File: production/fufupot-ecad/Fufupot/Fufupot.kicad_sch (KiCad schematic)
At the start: 56 parts, among them IC1 FOD3150, J1 Conn_01x04_Pin, J1 USB_B, J10 Conn_01x03, J3 Conn_01x03, J4 Conn_01x02_Pin, J5 Conn_01x02_Pin, J6 Conn_01x03_Pin, J7 Conn_01x02_Pin, J9 Conn_01x04_Pin, SW1 SW_Push, U1 STGP8NC60KD, U2 FT232RL, U2 LM5165DRC, U3 USBLC6-2SC6, U4 ATMEGA328P-PN

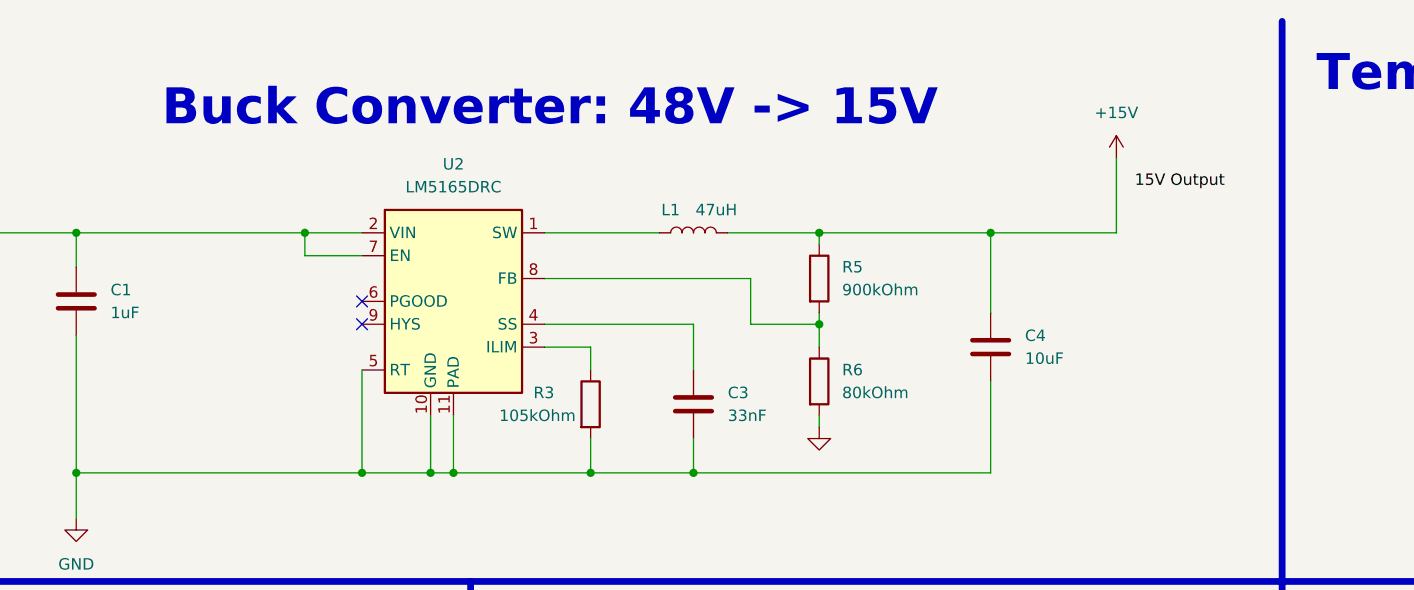
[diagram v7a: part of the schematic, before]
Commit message: Power Symbol and footprints
Made +16V power symbol and added footprints.
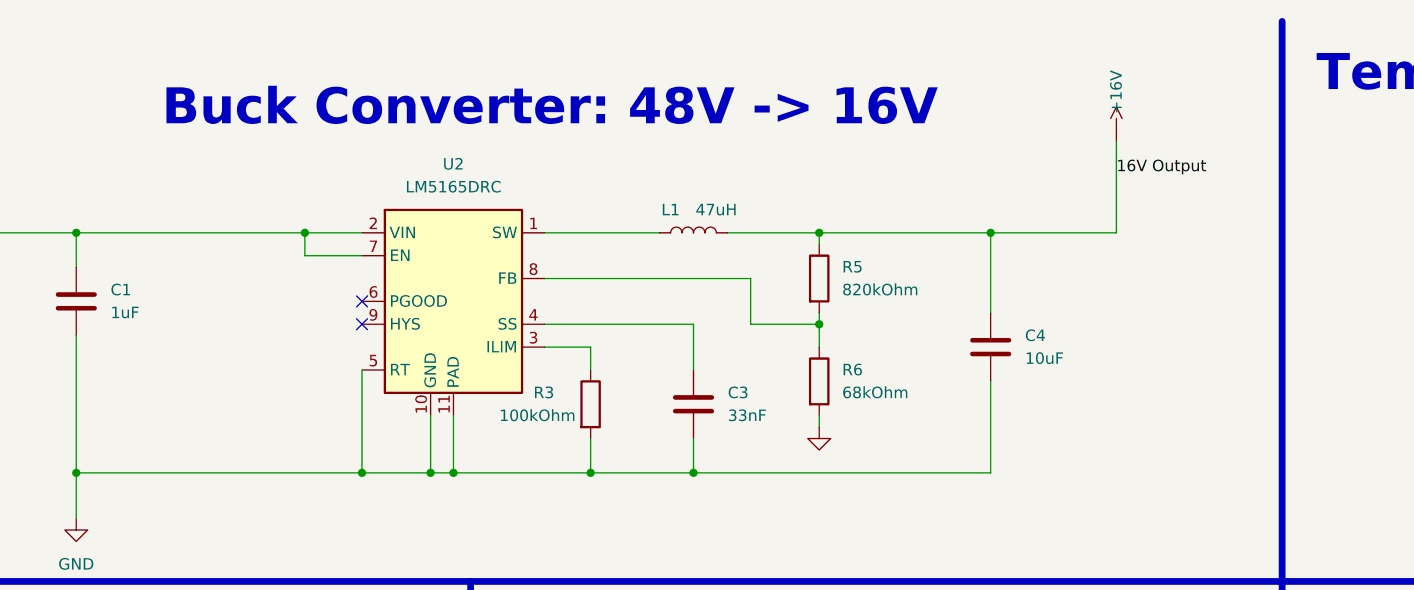
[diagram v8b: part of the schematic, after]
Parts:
- C1, C3, C4: footprint (none) -> Capacitor_SMD:C_0805_2012Metric
- L1: footprint (none) -> Inductor_SMD:L_0805_2012Metric
- R3: value 105kOhm -> 100kOhm; footprint (none) -> Resistor_SMD:R_0805_2012Metric
- R5: value 900kOhm -> 820kOhm; footprint (none) -> Resistor_SMD:R_0805_2012Metric
- R6: value 80kOhm -> 68kOhm; footprint (none) -> Resistor_SMD:R_0805_2012Metric
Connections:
- net +15V: no longer C4.1, L1.2, R5.1
- new net +16V: C4.1, L1.2, R5.1
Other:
- note added: "Buck Converter: 48V -> 16V"
- note removed: "Buck Converter: 48V -> 15V"
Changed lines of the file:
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@@
     (stroke (width 0) (type default))
   )
-  (wire (pts (xy 212.09 27.305) (xy 212.09 35.56))
+  (wire (pts (xy 212.09 25.4) (xy 212.09 35.56))
     (stroke (width 0) (type default))
   )
@@
     (effects (font (size 4 4) (thickness 0.6) bold) (justify left bottom))
   )
-  (text "Buck Converter: 48V -> 15V" (at 106.045 24.13 0)
+  (text "Buck Converter: 48V -> 16V" (at 106.045 24.13 0)
     (effects (font (size 4 4) (thickness 0.6) bold) (justify left bottom))
   )
@@
     (effects (font (size 4 4) (thickness 0.8) bold) (justify left bottom))
   )
-  (label "15V Output" (at 214.122 30.734 0) (fields_autoplaced)
+  (label "16V Output" (at 212.09 29.21 0) (fields_autoplaced)
     (effects (font (size 1.27 1.27)) (justify left bottom))
   )
@@
       (effects (font (size 1.27 1.27)) (justify left))
     )
-    (property "Footprint" "" (at 97.4852 46.99 0)
+    (property "Footprint" "Capacitor_SMD:C_0805_2012Metric" (at 97.4852 46.99 0)
       (effects (font (size 1.27 1.27)) hide)
     )
@@
     )
   )
-  (symbol (lib_id "power:+15V") (at 212.09 27.305 0) (unit 1)
-    (in_bom yes) (on_board yes) (dnp no) (fields_autoplaced)
-    (property "Reference" "#PWR05" (at 212.09 31.115 0)
-      (effects (font (size 1.27 1.27)) hide)
-    )
-    (property "Value" "+15V" (at 212.09 22.225 0)
-      (effects (font (size 1.27 1.27)))
-    )
-    (property "Footprint" "" (at 212.09 27.305 0)
-      (effects (font (size 1.27 1.27)) hide)
-    )
-    (property "Datasheet" "" (at 212.09 27.305 0)
-      (effects (font (size 1.27 1.27)) hide)
-    )
-    (pin "1")
-    (instances
-      (project "Induction Heating"
-        (path "/66a13b46-c5dd-4058-93db-41d44d6afefc"
-          (reference "#PWR05") (unit 1)
-        )
-      )
-      (project "Fufupot"
-        (path "/e8bc21b1-eda8-45a8-be25-55b90339183f"
-          (reference "#PWR028") (unit 1)
-        )
-      )
-    )
-  )
   (symbol (lib_id "power:+3V3") (at 154.432 196.215 0) (unit 1)
     (in_bom yes) (on_board yes) (dnp no) (fields_autoplaced)
@@
       (effects (font (size 1.27 1.27)) (justify left))
     )
-    (property "Value" "80kOhm" (at 181.61 53.34 0)
+    (property "Value" "68kOhm" (at 181.61 53.34 0)
       (effects (font (size 1.27 1.27)) (justify left))
     )
-    (property "Footprint" "" (at 177.292 52.07 90)
+    (property "Footprint" "Resistor_SMD:R_0805_2012Metric" (at 177.292 52.07 90)
       (effects (font (size 1.27 1.27)) hide)
     )
@@
     )
   )
+  (symbol (lib_id "more_powerSymbols:+16V") (at 212.09 25.4 0) (unit 1)
+    (in_bom no) (on_board no) (dnp no) (fields_autoplaced)
+    (property "Reference" "#PWR028" (at 212.09 20.32 0)
+      (effects (font (size 1.27 1.27)) hide)
+    )
+    (property "Value" "~" (at 212.09 25.4 0)
+      (effects (font (size 1.27 1.27)))
+    )
+    (property "Footprint" "" (at 212.09 25.4 0)
+      (effects (font (size 1.27 1.27)) hide)
+    )
+    (property "Datasheet" "" (at 212.09 25.4 0)
+      (effects (font (size 1.27 1.27)) hide)
+    )
+    (pin "")
+    (instances
+      (project "Fufupot"
+        (path "/e8bc21b1-eda8-45a8-be25-55b90339183f"
+          (reference "#PWR028") (unit 1)
+        )
+      )
+    )
+  )
   (symbol (lib_id "Device:R") (at 278.765 112.395 90) (unit 1)
     (in_bom yes) (on_board yes) (dnp no) (fields_autoplaced)
@@
       (effects (font (size 1.27 1.27)) (justify left))
     )
-    (property "Footprint" "" (at 199.0852 52.07 0)
+    (property "Footprint" "Capacitor_SMD:C_0805_2012Metric" (at 199.0852 52.07 0)
       (effects (font (size 1.27 1.27)) hide)
     )
@@
       (effects (font (size 1.27 1.27)) (justify left))
     )
-    (property "Value" "105kOhm" (at 143.51 55.88 0)
+    (property "Value" "100kOhm" (at 143.51 55.88 0)
       (effects (font (size 1.27 1.27)) (justify left))
     )
-    (property "Footprint" "" (at 151.892 54.61 90)
+    (property "Footprint" "Resistor_SMD:R_0805_2012Metric" (at 151.892 54.61 90)
       (effects (font (size 1.27 1.27)) hide)
     )
@@
       (effects (font (size 1.27 1.27)) (justify left))
     )
-    (property "Value" "900kOhm" (at 181.61 41.91 0)
+    (property "Value" "820kOhm" (at 181.61 41.91 0)
       (effects (font (size 1.27 1.27)) (justify left))
     )
-    (property "Footprint" "" (at 177.292 40.64 90)
+    (property "Footprint" "Resistor_SMD:R_0805_2012Metric" (at 177.292 40.64 90)
       (effects (font (size 1.27 1.27)) hide)
     )
@@
       (effects (font (size 1.27 1.27)) (justify left))
     )
-    (property "Footprint" "" (at 166.0652 58.42 0)
+    (property "Footprint" "Capacitor_SMD:C_0805_2012Metric" (at 166.0652 58.42 0)
       (effects (font (size 1.27 1.27)) hide)
     )
@@
       (effects (font (size 1.27 1.27)))
     )
-    (property "Footprint" "" (at 165.1 35.56 0)
+    (property "Footprint" "Inductor_SMD:L_0805_2012Metric" (at 165.1 35.56 0)
       (effects (font (size 1.27 1.27)) hide)
     )
